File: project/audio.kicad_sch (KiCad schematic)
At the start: 0 parts

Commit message: Minor changes to audio design
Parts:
- added C107, C109, C110, C112, C114, C116: 0u1, symbol Device:C
- added C108, C111, C113, C115, C117: 1u, symbol Device:C
- added IC10: TLV320AIC3104IRHBR, QFN50P500X500X100-33N-D, symbol bozi:TLV320AIC3104IRHBR
- added R27, R28: TBD, symbol Device:R
- added U5: ~, symbol bozi:SPH0141LM4H-1
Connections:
- new net 3V3_SW: C107.1, C110.1, C111.1, C112.1, C113.1, C114.1, C115.1, C116.1, C117.1, IC10.18 (DRVDD_1), IC10.24 (DRVDD_2), IC10.25 (AVDD), IC10.7 (IOVDD), R27.1, R28.1, U5.2 (SEL), U5.5 (VDD)
- new net BCLK: IC10.2 (BCLK)
- new net GNDREF: C107.2, C108.2, C109.2, C110.2, C111.2, C112.2, C113.2, C114.2, C115.2, C116.2, C117.2, IC10.17 (AVSS1), IC10.21 (DRVSS), IC10.26 (AVSS2), IC10.33 (EP), IC10.6 (DVSS), U5.3 (GND)
- new net I2C_SCL: IC10.8 (SCL), R27.2
- new net I2C_SDA: IC10.9 (SDA), R28.2
- new net MCLK: IC10.1 (MCLK)
- new net MIC_CLK: U5.4 (CLOCK)
- new net MIC_DATA: U5.1 (DATA)
- new net NRST: IC10.31 (~{RESET})
- new net RX: IC10.4 (DIN)
- new net TBD: C108.1, C109.1, IC10.32 (DVDD)
- new net TX: IC10.5 (DOUT)
- new net WCLK: IC10.3 (WCLK)
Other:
- note added: "Audio serial data bus bit clock input/output"
- note added: "Audio serial data bus word clock input/output"
- note added: "Master clock input"
- note added: "codec"
- note added: "microphone"

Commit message: schemtic is done, need to go through BOM
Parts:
- added C118, C124: TBD, symbol Device:C
- added C119: 0.1uF, symbol Device:C
- added IC11: TPA2005D1DGNR, SOP65P490X110-9N, symbol bozi:TPA2005D1DGNR
- added J5: CTIA, symbol bozi:AUDIO-JACK_(CTIA)_4_PIN
- added LS1: Speaker, TBD, symbol Device:Speaker
- added R29, R30: TBD, symbol Device:R
- added R47: 1k, symbol Device:R
- added R64, R65, R66, R67, R68, R69, R70, R80, R81, R82, R83: 0R, bozi:RESC1005X37N_edit, symbol Device:R
- added U6: TBD, symbol bozi:XO_(OSCILLATOR)
- C106: renamed from C107; value 0u1 -> 100nF; footprint (none) -> bozi:GRM18_T10; Manufacturer_Name (none) -> Murata Electronics; Manufacturer_Part_Number (none) -> GRM188R71H104KA93D
- C107: renamed from C114; value 0u1 -> 100nF; footprint (none) -> bozi:GRM18_T10; Manufacturer_Name (none) -> Murata Electronics; Manufacturer_Part_Number (none) -> GRM188R71H104KA93D
- C108: renamed from C115; value 1u -> 1uF; footprint (none) -> bozi:GRM15_T05; Manufacturer_Name (none) -> Murata Electronics; Manufacturer_Part_Number (none) -> GRM155R61E105KA12D
- C109: renamed from C116; value 0u1 -> 100nF; footprint (none) -> bozi:GRM18_T10; Manufacturer_Name (none) -> Murata Electronics; Manufacturer_Part_Number (none) -> GRM188R71H104KA93D
- C110: renamed from C117; value 1u -> 1uF; footprint (none) -> bozi:GRM15_T05; Manufacturer_Name (none) -> Murata Electronics; Manufacturer_Part_Number (none) -> GRM155R61E105KA12D
- C111: renamed from C112; value 0u1 -> 100nF; footprint (none) -> bozi:GRM18_T10; Manufacturer_Name (none) -> Murata Electronics; Manufacturer_Part_Number (none) -> GRM188R71H104KA93D
- C112: renamed from C113; value 1u -> 1uF; footprint (none) -> bozi:GRM15_T05; Manufacturer_Name (none) -> Murata Electronics; Manufacturer_Part_Number (none) -> GRM155R61E105KA12D
- C113: renamed from C110; value 0u1 -> 100nF; footprint (none) -> bozi:GRM18_T10; Manufacturer_Name (none) -> Murata Electronics; Manufacturer_Part_Number (none) -> GRM188R71H104KA93D
- C114: renamed from C111; value 1u -> 1uF; footprint (none) -> bozi:GRM15_T05; Manufacturer_Name (none) -> Murata Electronics; Manufacturer_Part_Number (none) -> GRM155R61E105KA12D
- C115: renamed from C109; value 0u1 -> 100nF; footprint (none) -> bozi:GRM18_T10; Manufacturer_Name (none) -> Murata Electronics; Manufacturer_Part_Number (none) -> GRM188R71H104KA93D
- C116: renamed from C108; value 1u -> 1uF; footprint (none) -> bozi:GRM15_T05; Manufacturer_Name (none) -> Murata Electronics; Manufacturer_Part_Number (none) -> GRM155R61E105KA12D
- R24: renamed from R27; Manufacturer_Name (none) -> Yageo
- R25: renamed from R28; Manufacturer_Name (none) -> Yageo
- U4: renamed from U5; value ~ -> Microphone; footprint (none) -> TBD; Manufacturer_Name (none) -> Syntiant; Manufacturer_Part_Number (none) -> SPH0141LM4H-1
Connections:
- net 3V3_SW: now also R64.2, R65.2, R66.2, R67.1, R68.2; no longer C106.1, C107.1, C108.1, C109.1, C110.1, C111.1, C112.1, C113.1, C114.1, IC10.18 (DRVDD_1), IC10.24 (DRVDD_2), IC10.25 (AVDD), IC10.7 (IOVDD), U4.2 (SEL), U4.5 (VDD)
- net GNDREF: now also C124.2, IC11.7 (GND_1), IC11.9 (GND_2), U6.2 (GND)
- net TBD: now also R69.2; no longer C115.1, C116.1, IC10.32 (DVDD)
- net at IC10.14 (MIC2L/LINE2L/MICDET): now also C119.2, R47.2, R80.2, R83.2
- net at IC10.15 (MICBIAS): now also R47.1
- net at IC10.16 (MIC2R/LINE2R): now also C119.1
- net at IC10.19 (HPLOUT): now also J5.4 (L)
- net at IC10.20 (HPLCOM): now also IC10.22 (HPRCOM), R81.2, R82.2
- net at IC10.23 (HPROUT): now also J5.3 (R)
- net at IC10.29 (RIGHT_LOP): now also R29.1
- net at IC10.30 (RIGHT_LOM): now also R30.1
- net BCLK renamed I2S_BCLK
- net MCLK: no longer names the net of IC10.1 (MCLK)
- net MCLK: now also U6.3 (OUT)
- net RX renamed I2S_SDI
- net TX renamed I2S_SDO
- net WCLK renamed I2S_WCLK
- new net: C107.1, C108.1, C109.1, C110.1, IC10.18 (DRVDD_1), IC10.24 (DRVDD_2), R65.1
- new net: IC11.6 (VDD), R70.1
- new net: C106.1, R67.2, U4.2 (SEL), U4.5 (VDD)
- new net: C124.1, U6.1 (Tri-State)
- new net: C113.1, C114.1, IC10.7 (IOVDD), R68.1
- new net: C115.1, C116.1, IC10.32 (DVDD), R69.1
- new net: C111.1, C112.1, IC10.25 (AVDD), R66.1
- new net: IC11.5 (VO+), LS1.1
- new net: IC11.8 (VO-), LS1.2
- new net: R64.1, U6.4 (VDD)
- new net: C118.2, IC11.3 (IN+), R29.2
- new net: C118.1, IC11.4 (IN-), R30.2
- new net: J5.2 (GND), R81.1, R83.1
- new net: J5.1 (MIC), R80.1, R82.1
- new net VDD: IC11.1 (~{SHUTDOWN}), R70.2
- no-connect marks 0 -> 7
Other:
- note added: "4 Ohms"
- note added: "I2S_BCLK"
- note added: "I2S_MCLK"
- note added: "I2S_WCLK"
- note added: "Solder brdige for option between OMTP and CTIA. GND - MIC bridge"
- note added: "TBD if DRVDD needs a bulk capacitor of 10uF"
- note added: "This option allows for OMTP"
- note removed: "microphone"
- moved on the sheet: C106, C107, C108, C109, C110, C111, C112, C113, C114, C115, C116, IC10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

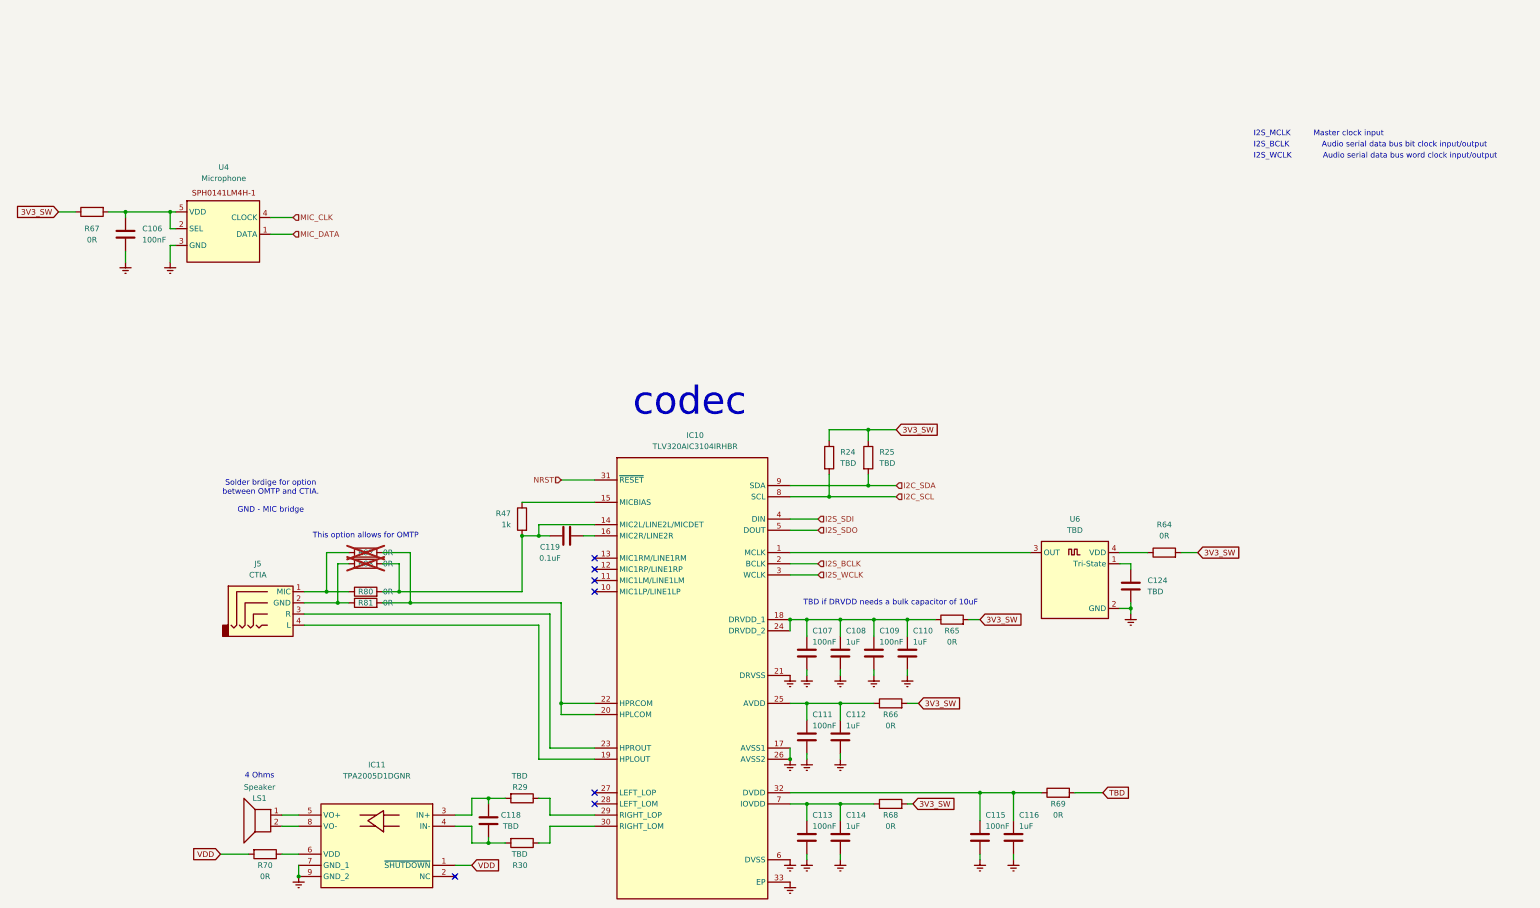
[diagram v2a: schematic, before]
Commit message: schemtic is done, annotation set
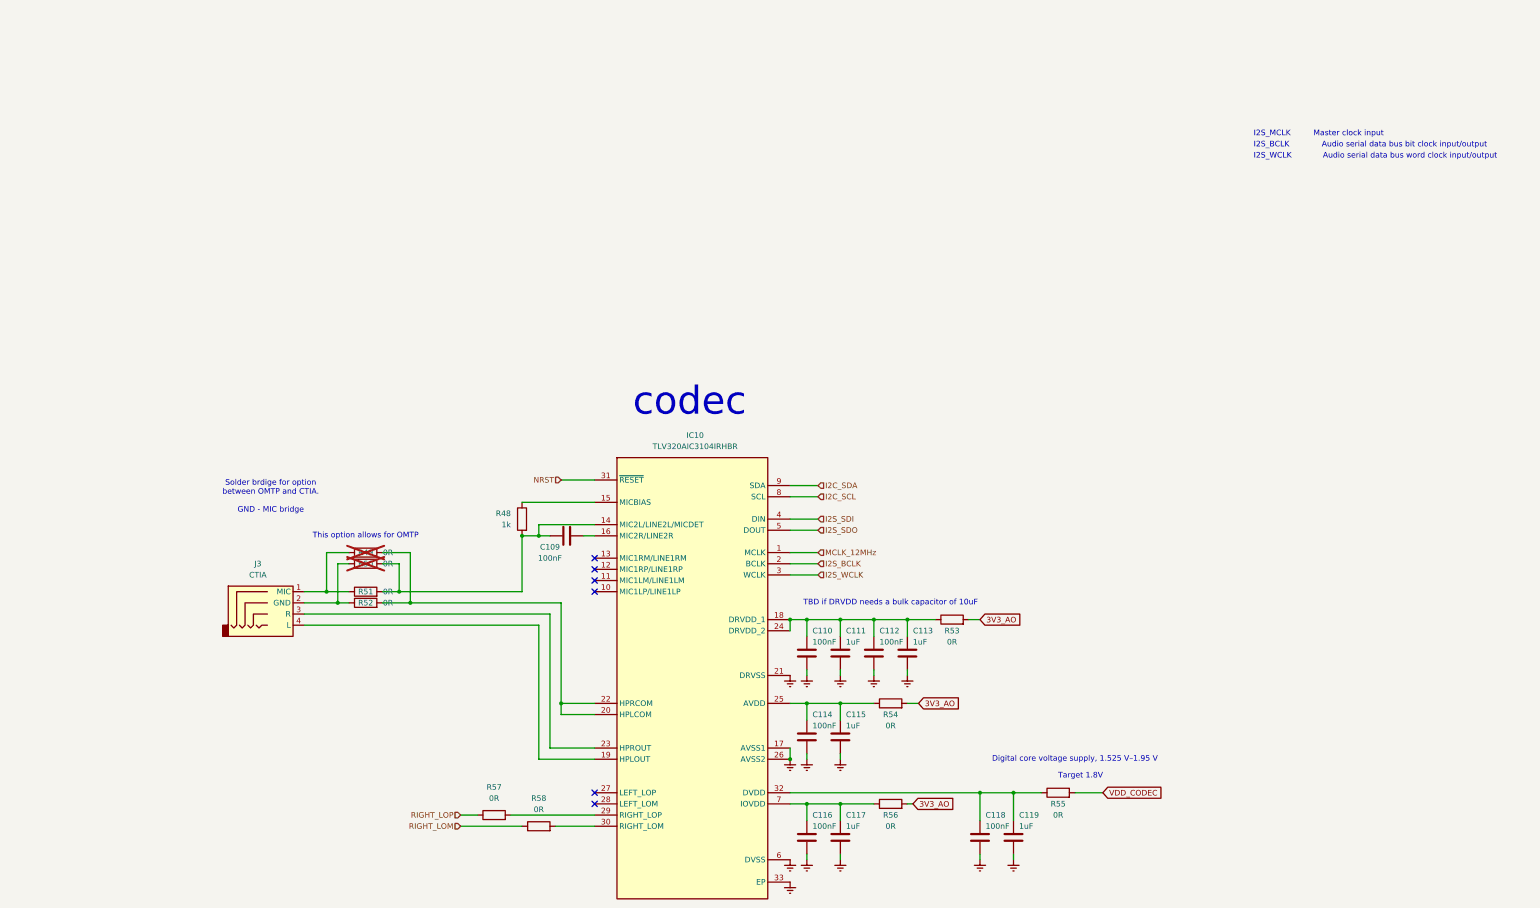
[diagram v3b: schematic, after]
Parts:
- removed C106: 100nF, bozi:GRM18_T10, symbol Device:C
- removed C118, C124: TBD, symbol Device:C
- removed IC11: TPA2005D1DGNR, SOP65P490X110-9N, symbol bozi:TPA2005D1DGNR
- removed LS1: Speaker, TBD, symbol Device:Speaker
- removed R24, R25, R29, R30: TBD, symbol Device:R
- removed R64, R67, R70: 0R, bozi:RESC1005X37N_edit, symbol Device:R
- removed U4: Microphone, TBD, symbol bozi:SPH0141LM4H-1
- removed U6: TBD, symbol bozi:XO_(OSCILLATOR)
- added R57, R58: 0R, bozi:RESC1005X37N_edit, symbol Device:R
- C109: renamed from C119; value 0.1uF -> 100nF; footprint (none) -> bozi:GRM18_T10; Manufacturer_Part_Number (none) -> GRM188R71H104KA93D
- J3: renamed from J5; footprint (none) -> bozi:SJ23574ASMTTR; Manufacturer_Name (none) -> Same Sky (Formerly CUI Devices); Manufacturer_Part_Number (none) -> SJ2-3574A-SMT-TR
- R48: renamed from R47; footprint (none) -> bozi:RESC1005X37N_edit; Manufacturer_Name Yageo -> YAGEO; Manufacturer_Part_Number (none) -> RT0402BRB071KL
- renumbered C107 to C110, C108 to C111, C109 to C112, C110 to C113, C111 to C114, C112 to C115, C113 to C116, C114 to C117, C115 to C118, C116 to C119, R82 to R49, R83 to R50, R80 to R51, R81 to R52, R65 to R53, R66 to R54, R69 to R55, R68 to R56
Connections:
- net MCLK_12MHz: now reaches IC10.1 (MCLK)
- net at IC10.29 (RIGHT_LOP): now also R57.2
- net at IC10.30 (RIGHT_LOM): now also R58.2
- net 3V3_SW renamed 3V3_AO
- net TBD renamed VDD_CODEC
- new net RIGHT_LOM: R58.1
- new net RIGHT_LOP: R57.1
- no-connect marks 7 -> 6
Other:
- note added: "Digital core voltage supply, 1.525 V–1.95 V"
- note added: "Target 1.8V"
- note removed: "4 Ohms"

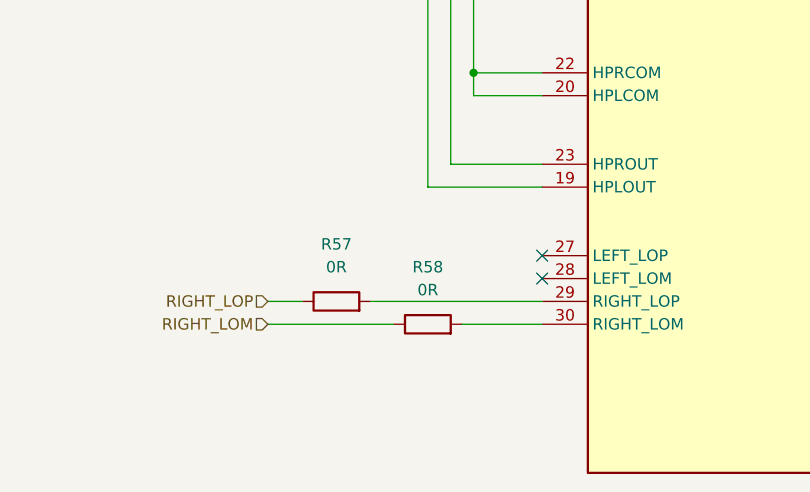
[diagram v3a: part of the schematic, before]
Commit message: PCB design, finished RAM, audio, battery fuel gauge and charger, PMIC, USB C power
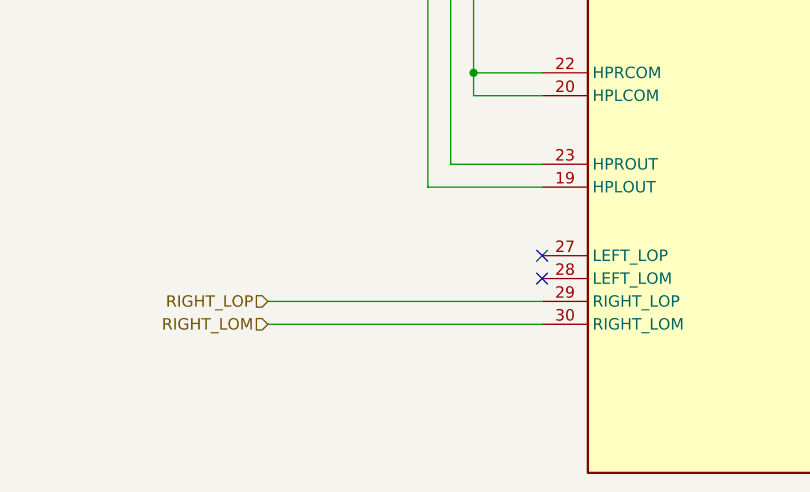
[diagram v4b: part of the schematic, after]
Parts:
- removed R57, R58: 0R, bozi:RESC1005X37N_edit, symbol Device:R
- IC10: footprint QFN50P500X500X100-33N-D -> bozi:QFN50P500X500X100-33N-D_edit
- J3: footprint bozi:SJ23574ASMTTR -> bozi:SJ23574ASMTTR_edit
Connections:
- net RIGHT_LOM: now also IC10.30 (RIGHT_LOM)
- net RIGHT_LOP: now also IC10.29 (RIGHT_LOP)
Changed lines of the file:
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@@
 	(wire
 		(pts
-			(xy 184.15 201.93) (xy 203.2 201.93)
-		)
-		(stroke
-			(width 0)
-			(type default)
-		)
-	)
-	(wire
-		(pts
 			(xy 259.08 199.39) (xy 266.7 199.39)
 		)
@@
 	(wire
 		(pts
-			(xy 172.72 201.93) (xy 176.53 201.93)
+			(xy 172.72 201.93) (xy 203.2 201.93)
 		)
 		(stroke
@@
 	(wire
 		(pts
-			(xy 172.72 204.47) (xy 186.69 204.47)
+			(xy 172.72 204.47) (xy 203.2 204.47)
 		)
 		(stroke
@@
 	(wire
 		(pts
-			(xy 194.31 204.47) (xy 203.2 204.47)
-		)
-		(stroke
-			(width 0)
-			(type default)
-		)
-	)
-	(wire
-		(pts
 			(xy 137.16 151.13) (xy 142.24 151.13)
 		)
@@
 	(symbol
 		(lib_id "Device:R")
-		(at 190.5 204.47 90)
-		(unit 1)
-		(exclude_from_sim no)
-		(in_bom yes)
-		(on_board yes)
-		(dnp no)
-		(fields_autoplaced yes)
-		(property "Reference" "R58"
-			(at 190.5 198.12 90)
-			(effects
-				(font
-					(size 1.27 1.27)
-				)
-			)
-		)
-		(property "Value" "0R"
-			(at 190.5 200.66 90)
-			(effects
-				(font
-					(size 1.27 1.27)
-				)
-			)
-		)
-		(property "Footprint" "bozi:RESC1005X37N_edit"
-			(at 190.5 206.248 90)
-			(effects
-				(font
-					(size 1.27 1.27)
-				)
-				(hide yes)
-			)
-		)
-		(property "Datasheet" "~"
-			(at 190.5 204.47 0)
-			(effects
-				(font
-					(size 1.27 1.27)
-				)
-				(hide yes)
-			)
-		)
-		(property "Description" "Resistor"
-			(at 190.5 204.47 0)
-			(effects
-				(font
-					(size 1.27 1.27)
-				)
-				(hide yes)
-			)
-		)
-		(property "Manufacturer_Name" "YAGEO"
-			(at 190.5 204.47 90)
-			(effects
-				(font
-					(size 1.27 1.27)
-				)
-				(hide yes)
-			)
-		)
-		(property "Manufacturer_Part_Number" "RC0402JR-070RL"
-			(at 190.5 204.47 90)
-			(effects
-				(font
-					(size 1.27 1.27)
-				)
-				(hide yes)
-			)
-		)
-		(pin "2"
-		)
-		(pin "1"
-		)
-		(instances
-			(project "project"
-				(path "/7afeae28-8837-445b-b53a-5d89eb16eb45/e5d9d73d-3ae6-40b8-8194-94dccca16526"
-					(reference "R58")
-					(unit 1)
-				)
-			)
-		)
-	)
-	(symbol
-		(lib_id "Device:R")
 		(at 151.13 144.78 90)
 		(unit 1)
@@
 	)
 	(symbol
-		(lib_id "Device:R")
-		(at 180.34 201.93 90)
-		(unit 1)
-		(exclude_from_sim no)
-		(in_bom yes)
-		(on_board yes)
-		(dnp no)
-		(fields_autoplaced yes)
-		(property "Reference" "R57"
-			(at 180.34 195.58 90)
-			(effects
-				(font
-					(size 1.27 1.27)
-				)
-			)
-		)
-		(property "Value" "0R"
-			(at 180.34 198.12 90)
-			(effects
-				(font
-					(size 1.27 1.27)
-				)
-			)
-		)
-		(property "Footprint" "bozi:RESC1005X37N_edit"
-			(at 180.34 203.708 90)
-			(effects
-				(font
-					(size 1.27 1.27)
-				)
-				(hide yes)
-			)
-		)
-		(property "Datasheet" "~"
-			(at 180.34 201.93 0)
-			(effects
-				(font
-					(size 1.27 1.27)
-				)
-				(hide yes)
-			)
-		)
-		(property "Description" "Resistor"
-			(at 180.34 201.93 0)
-			(effects
-				(font
-					(size 1.27 1.27)
-				)
-				(hide yes)
-			)
-		)
-		(property "Manufacturer_Name" "YAGEO"
-			(at 180.34 201.93 90)
-			(effects
-				(font
-					(size 1.27 1.27)
-				)
-				(hide yes)
-			)
-		)
-		(property "Manufacturer_Part_Number" "RC0402JR-070RL"
-			(at 180.34 201.93 90)
-			(effects
-				(font
-					(size 1.27 1.27)
-				)
-				(hide yes)
-			)
-		)
-		(pin "2"
-		)
-		(pin "1"
-		)
-		(instances
-			(project ""
-				(path "/7afeae28-8837-445b-b53a-5d89eb16eb45/e5d9d73d-3ae6-40b8-8194-94dccca16526"
-					(reference "R57")
-					(unit 1)
-				)
-			)
-		)
-	)
-	(symbol
 		(lib_id "Device:C")
 		(at 259.08 165.1 0)
@@
 			)
 		)
-		(property "Footprint" "bozi:SJ23574ASMTTR"
+		(property "Footprint" "bozi:SJ23574ASMTTR_edit"
 			(at 128.27 147.32 0)
 			(effects
@@
 			)
 		)
-		(property "Footprint" "QFN50P500X500X100-33N-D"
+		(property "Footprint" "bozi:QFN50P500X500X100-33N-D_edit"
 			(at 257.81 235.89 0)
 			(effects
